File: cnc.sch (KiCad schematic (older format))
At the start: 8 parts, among them CON1 SD_Card, U1 pic32

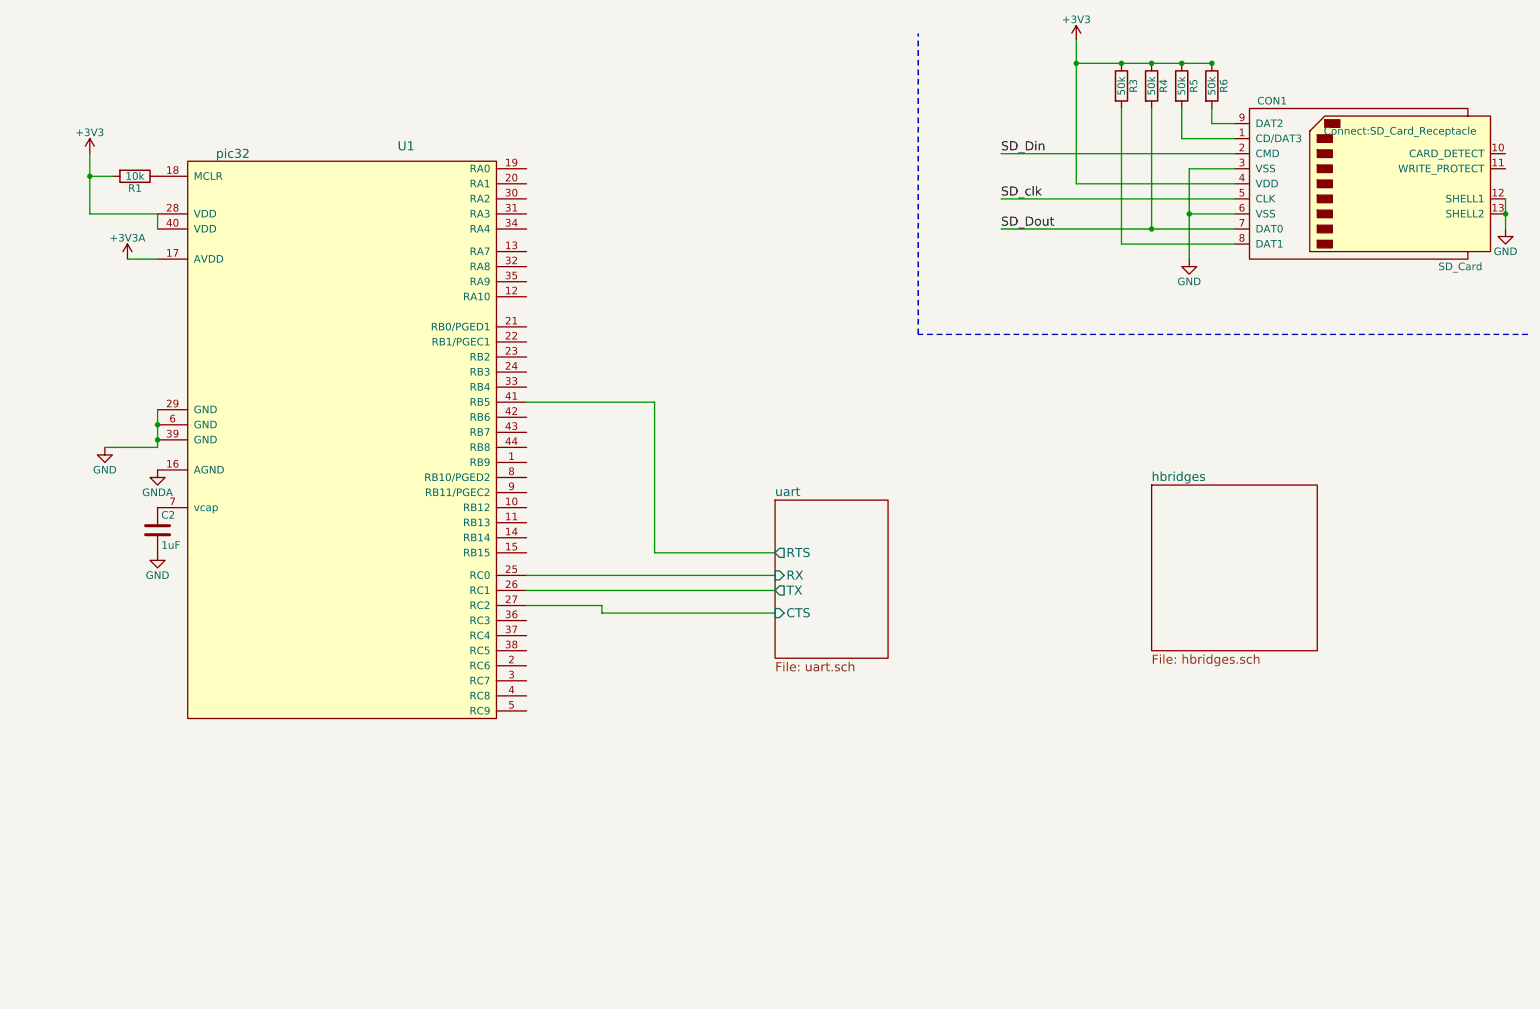
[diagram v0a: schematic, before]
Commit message: added 3 more h-bridges, and routed a bit
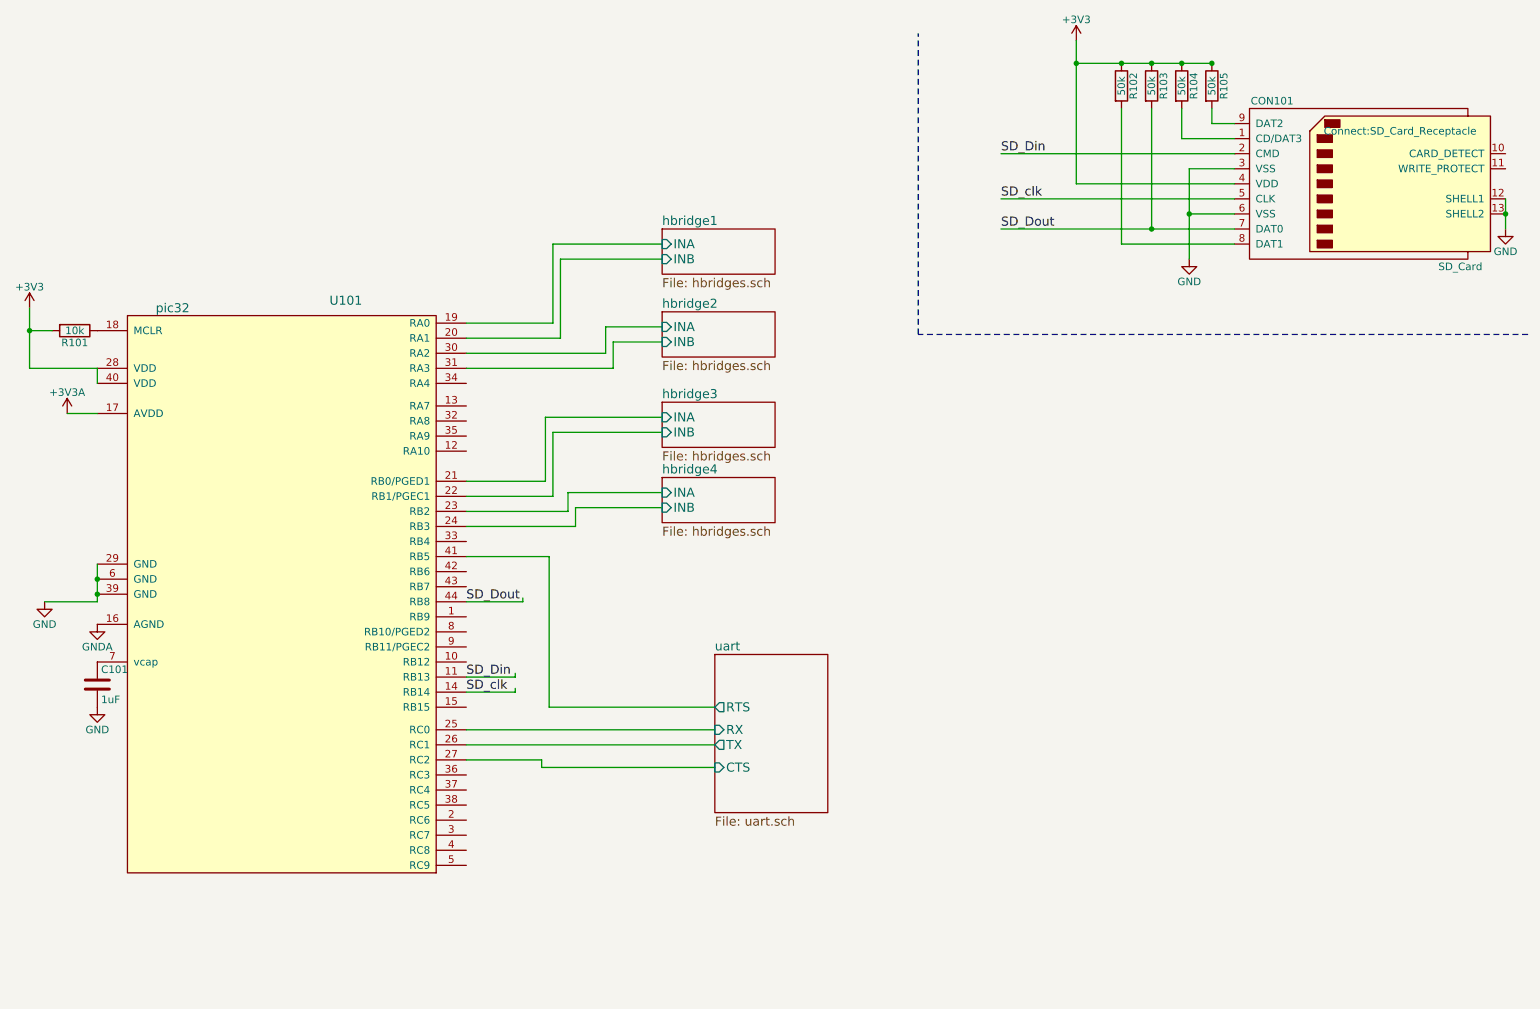
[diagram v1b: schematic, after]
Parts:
- renumbered C2 to C101, CON1 to CON101, R1 to R101, R3 to R102, R4 to R103, R5 to R104, R6 to R105, U1 to U101
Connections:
- wire segments 32 -> 62
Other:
- moved on the sheet: C101, R101, U101

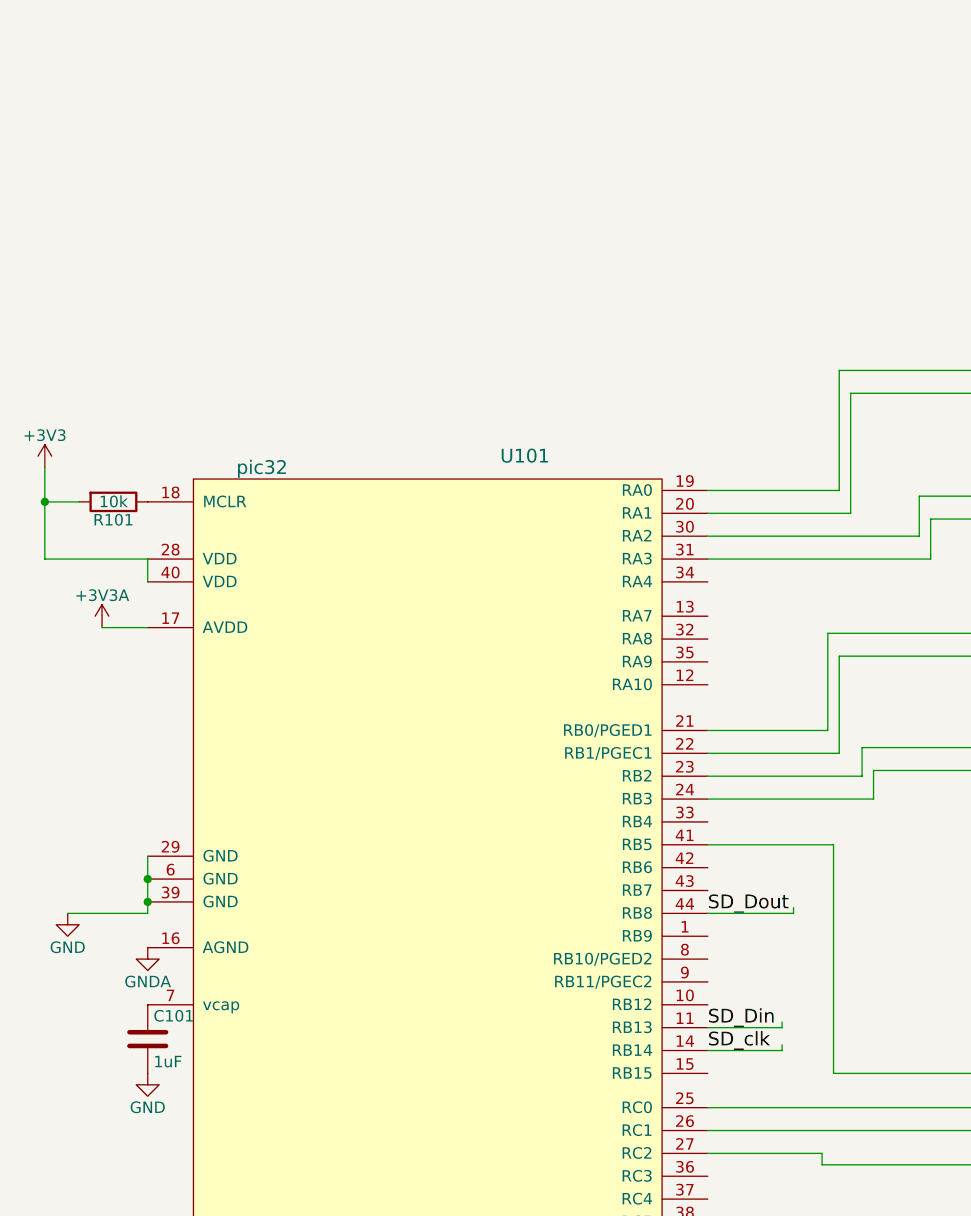
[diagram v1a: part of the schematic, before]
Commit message: Added requirements
Also selected components for certain things.
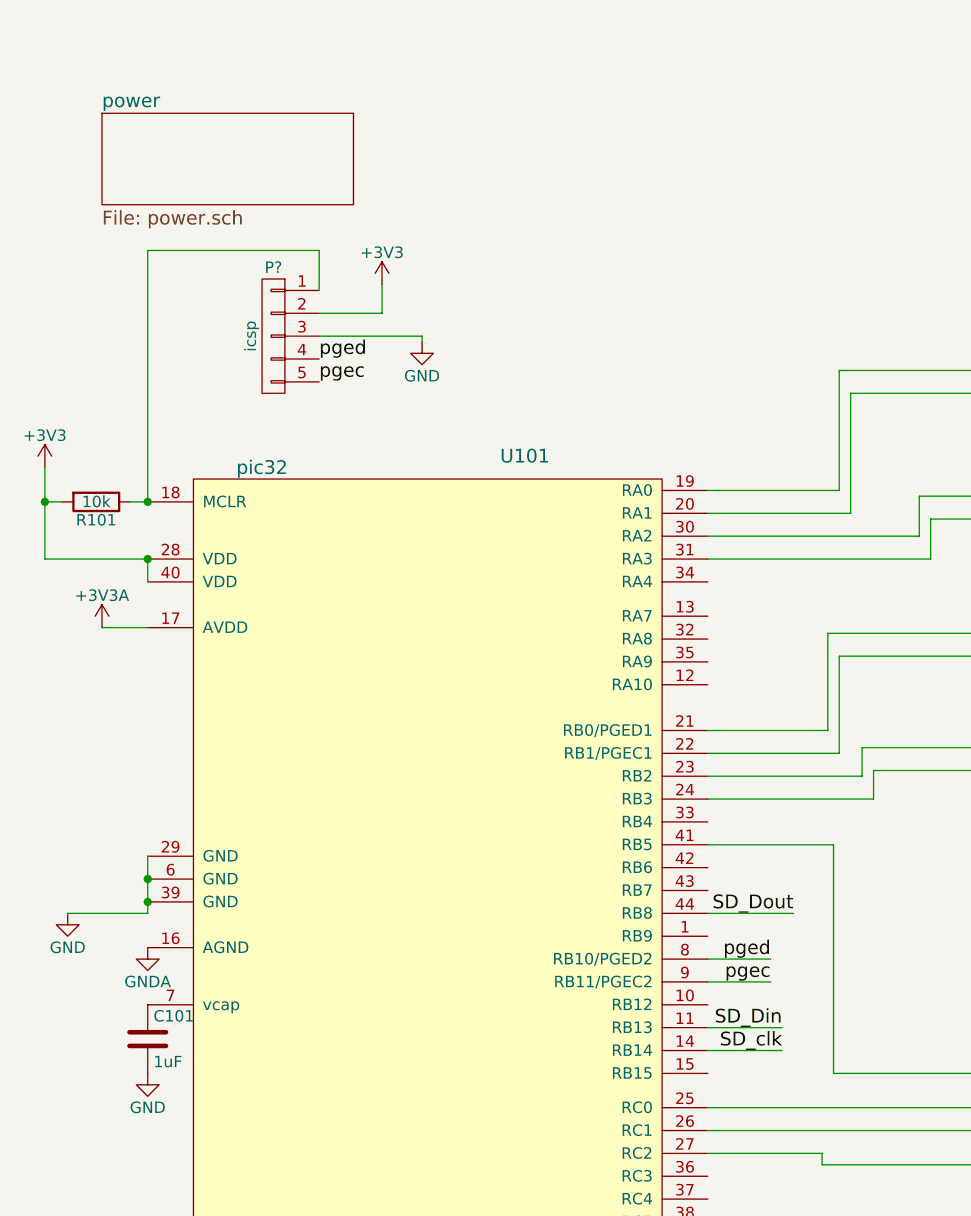
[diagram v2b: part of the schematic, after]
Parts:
- added P?: icsp, symbol CONN_01X05
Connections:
- net labels added: pgec, pged
- wire segments 62 -> 69
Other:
- moved on the sheet: R101
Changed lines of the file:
@@
 $Descr A4 11693 8268
 encoding utf-8
-Sheet 1 6
+Sheet 1 7
 Title ""
 Date ""
@@
 L R R101
 U 1 1 571B4082
-P 1400 2675
-F 0 "R101" V 1480 2675 50  0000 C CNN
-F 1 "10k" V 1400 2675 50  0000 C CNN
-F 2 "Resistors_SMD:R_0805_HandSoldering" V 1330 2675 50  0001 C CNN
-F 3 "" H 1400 2675 50  0000 C CNN
-	1    1400 2675
+P 1325 2675
+F 0 "R101" V 1405 2675 50  0000 C CNN
+F 1 "10k" V 1325 2675 50  0000 C CNN
+F 2 "Resistors_SMD:R_0805_HandSoldering" V 1255 2675 50  0001 C CNN
+F 3 "" H 1325 2675 50  0000 C CNN
+	1    1325 2675
 	0    1    1    0
 $EndComp
@@
 	1100 2525 1100 2925
 Wire Wire Line
-	1100 2675 1250 2675
-Wire Wire Line
 	1100 2925 1550 2925
 Connection ~ 1100 2675
@@
 Wire Wire Line
 	4725 3975 4000 3975
-Text Label 4000 4475 0    60   ~ 0
+Text Label 4375 4475 2    60   ~ 0
 SD_Dout
-Text Label 4000 5075 0    60   ~ 0
+Text Label 4325 5075 2    60   ~ 0
 SD_clk
-Text Label 4000 4975 0    60   ~ 0
+Text Label 4325 4975 2    60   ~ 0
 SD_Din
 Wire Wire Line
 	4000 4975 4325 4975
 Wire Wire Line
-	4325 4975 4325 4950
-Wire Wire Line
 	4000 5075 4325 5075
 Wire Wire Line
-	4325 5075 4325 5050
-Wire Wire Line
 	4000 4475 4375 4475
-Wire Wire Line
-	4375 4475 4375 4450
+$Sheet
+S 1350 975  1100 400
+U 57BD82CE
+F0 "power" 60
+F1 "power.sch" 60
+$EndSheet
+$Comp
+L CONN_01X05 P?
+U 1 1 57BDB89F
+P 2100 1950
+F 0 "P?" H 2100 2250 50  0000 C CNN
+F 1 "icsp" V 2200 1950 50  0000 C CNN
+F 2 "" H 2100 1950 50  0000 C CNN
+F 3 "" H 2100 1950 50  0000 C CNN
+	1    2100 1950
+	-1   0    0    -1
+$EndComp
+Wire Wire Line
+	1550 2675 1550 1575
+Wire Wire Line
+	1550 1575 2300 1575
+Wire Wire Line
+	2300 1575 2300 1750
+$Comp
+L +3V3 #PWR?
+U 1 1 57BDBEA3
+P 2575 1725
+F 0 "#PWR?" H 2575 1575 50  0001 C CNN
+F 1 "+3V3" H 2575 1865 50  0000 C CNN
+F 2 "" H 2575 1725 50  0000 C CNN
+F 3 "" H 2575 1725 50  0000 C CNN
+	1    2575 1725
+	1    0    0    -1
+$EndComp
+Wire Wire Line
+	2300 1850 2575 1850
+Wire Wire Line
+	2575 1850 2575 1725
+Wire Wire Line
+	1100 2675 1175 2675
+Wire Wire Line
+	1550 2675 1475 2675
+Connection ~ 1550 2675
+Connection ~ 1550 2925
+$Comp
+L GND #PWR?
+U 1 1 57BDC589
+P 2750 1975
+F 0 "#PWR?" H 2750 1725 50  0001 C CNN
+F 1 "GND" H 2750 1825 50  0000 C CNN
+F 2 "" H 2750 1975 50  0000 C CNN
+F 3 "" H 2750 1975 50  0000 C CNN
+	1    2750 1975
+	1    0    0    -1
+$EndComp
+Wire Wire Line
+	2300 1950 2750 1950
+Wire Wire Line
+	2750 1950 2750 1975
+Text Label 2300 2050 0    60   ~ 0
+pged
+Text Label 2300 2150 0    60   ~ 0
+pgec
+Text Label 4275 4675 2    60   ~ 0
+pged
+Text Label 4275 4775 2    60   ~ 0
+pgec
+Wire Wire Line
+	4000 4675 4275 4675
+Wire Wire Line
+	4000 4775 4275 4775
 $EndSCHEMATC
